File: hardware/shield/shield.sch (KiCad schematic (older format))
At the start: 30 parts, among them J10 10118193-0001LF, U1 LM1117, Y1 Crystal

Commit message: New version of shield.
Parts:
- removed C4: 22u, shield:SPARKFUN-CAPACITORS_AXIAL-5MM, symbol SPARKFUN-CAPACITORS_CAP
- removed R1, R2: 10k, shield:SPARKFUN-PASSIVES_0603-RES, symbol SPARKFUN-PASSIVES_RESISTOR
- removed U$2, U$3: TXS0101DBVR, shield:TEXAS_SOT-23-6, symbol TEXAS_TXS0101DBVR
- added C4: 22u, Capacitors_THT:C_Radial_D5_L6_P2.5, symbol CP
- added U2: 4052, Housings_SOIC:SOIC-16_3.9x9.9mm_Pitch1.27mm, symbol 4052
- added U3: TXB0104, Housings_SOIC:SOIC-14_3.9x8.7mm_Pitch1.27mm, symbol TXB0104
- JP1: value 3v3Src1 -> ~
- JP2: value 3v3Src2 -> ~
- PROG0: value PROG0 -> ~
- PROG1: value PROG1 -> ~
- PWR0: value PWR0 -> ~
- U$1: value CH340G -> ~
- Y1: value Crystal -> 12M
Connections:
- net labels added: D+, D-, RX, TX, XO
- net labels removed: N$1, N$3, N$43, N$46, N$49, N$5
- wire segments 193 -> 195
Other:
- moved on the sheet: E1

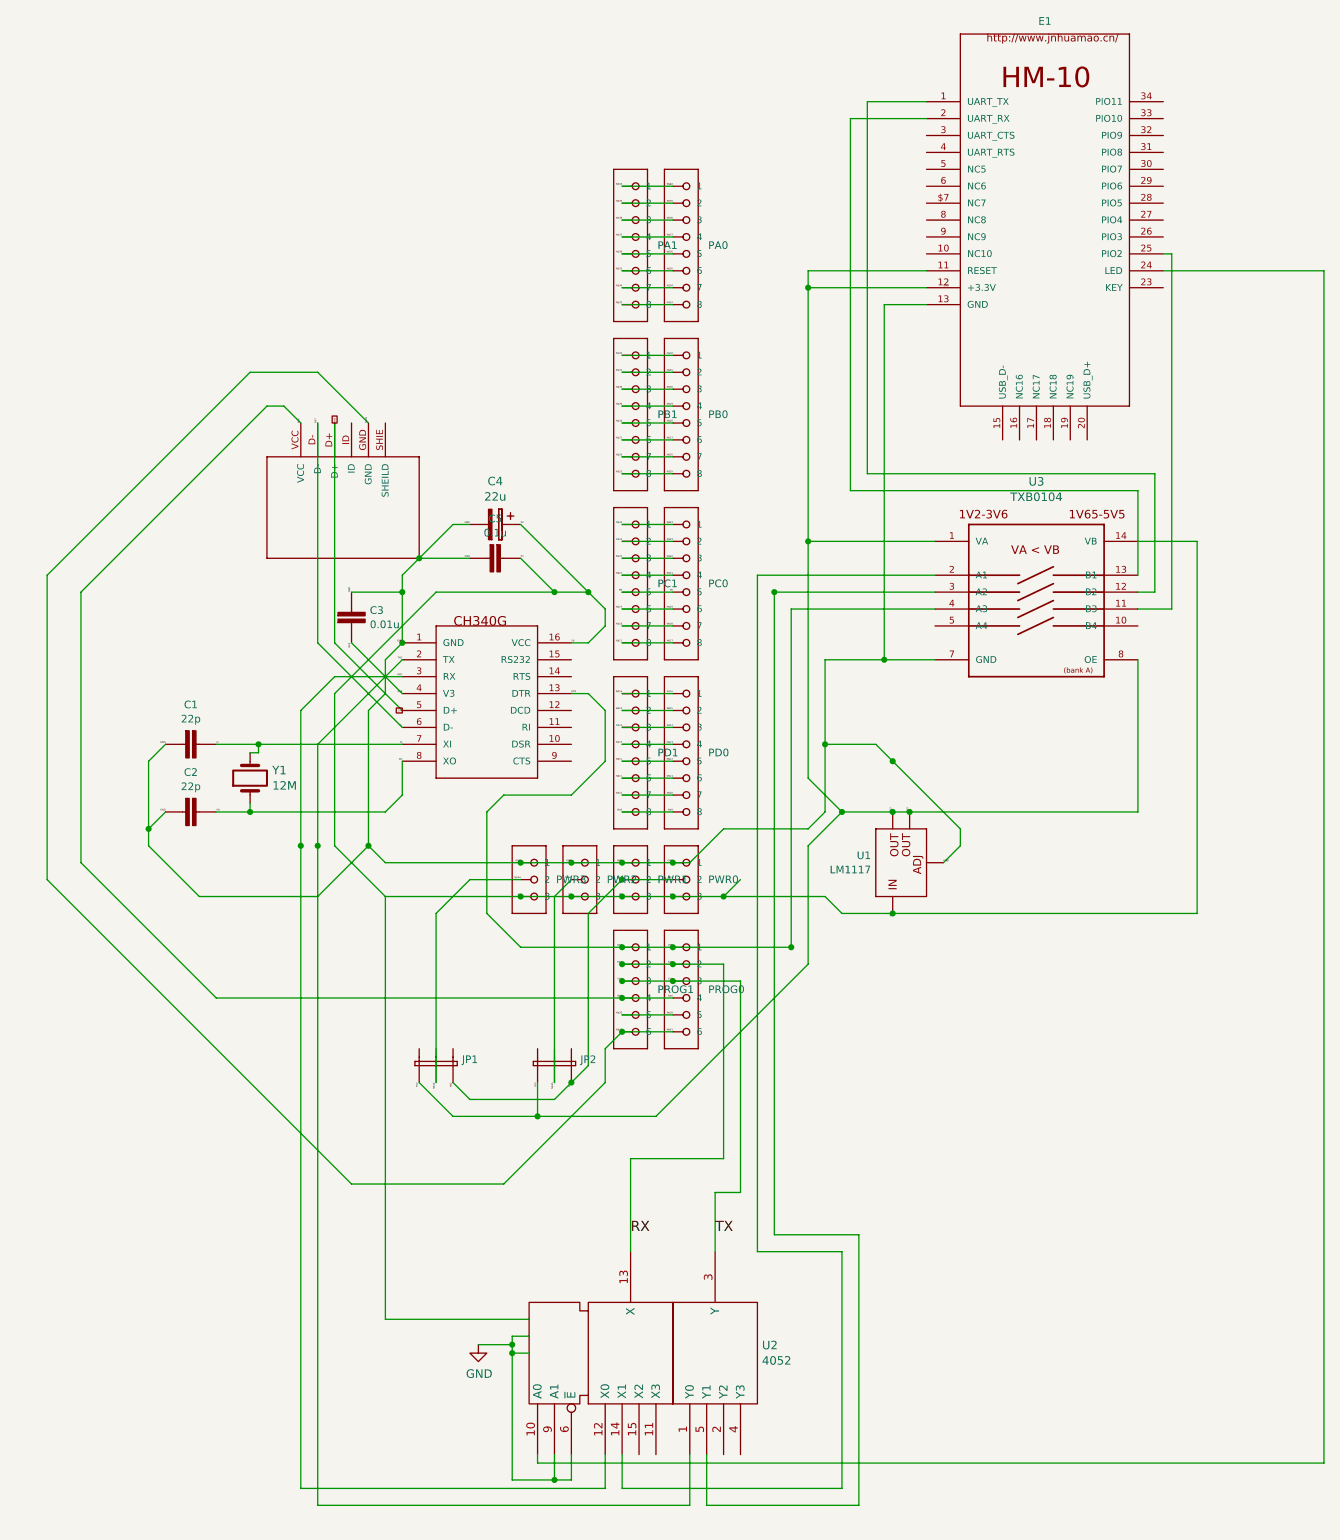
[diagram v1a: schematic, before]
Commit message: Fully-routed; just the wrong size.
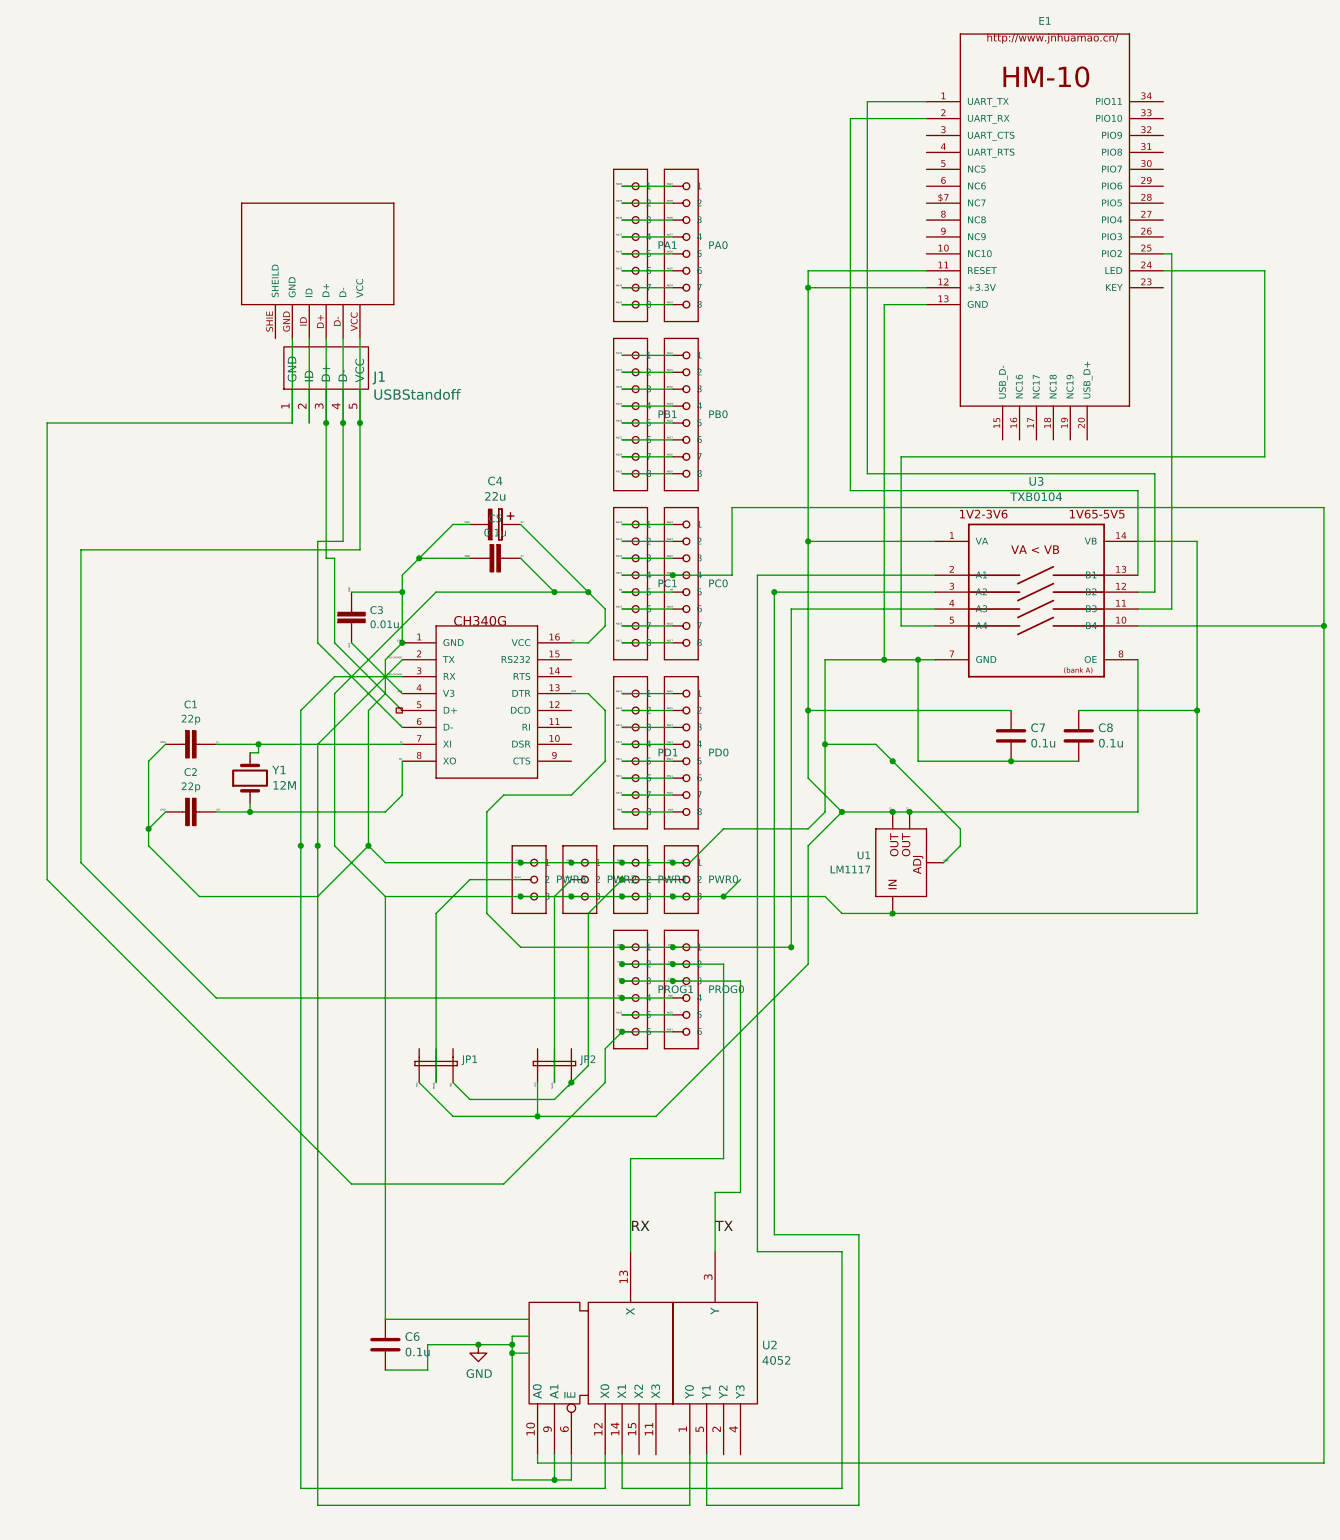
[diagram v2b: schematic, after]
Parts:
- added C6, C7, C8: 0.1u, Capacitors_SMD:C_0603_HandSoldering, symbol C
- added J1: USBStandoff, Pin_Headers:Pin_Header_Straight_1x05, symbol USBStandoff
- C1, C2, C3, C5: footprint shield:SPARKFUN-CAPACITORS_0603-CAP -> Capacitors_SMD:C_0603_HandSoldering
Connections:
- net 3V3: now also C7.1
- net D+: now also J1.3 (D+)
- net D-: now also J1.4 (D-)
- net GND: now also C6.2, C7.2, C8.2
- net N$21: now also U2.10 (A0), U3.10 (B4)
- net N$41: now also J1.1 (GND)
- net N$6: now also J1.5 (VCC)
- net RX: no longer U$1.3 (RX), U2.12 (X0)
- net TX: no longer U$1.2 (TX), U2.1 (Y0)
- net Vdd: now also C6.1, C8.1
- net at J10.ID: now also J1.2 (ID)
- net at E1.24 (LED): now also U3.5 (A4); no longer U2.10 (A0)
- new net RXD-CH340G: U$1.3 (RX), U2.12 (X0)
- new net TXD-CH340G: U$1.2 (TX), U2.1 (Y0)
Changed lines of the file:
@@
 L 10118193-0001LF_10118193-0001LF J10
 U 1 1 58543665
-P 9000 6550
-F 0 "J10" H 8990 6540 65  0001 L TNN
-F 1 "10118193-0001LF" H 8990 6440 65  0001 L TNN
-F 2 "shield:10118193-0001LF_10118193-0001LF" H 8990 6340 65  0001 L TNN
-F 3 "" H 9000 6550 60  0001 C CNN
-	1    9000 6550
-	0    -1   -1   0
+P 8950 5250
+F 0 "J10" H 8940 5240 65  0001 L TNN
+F 1 "10118193-0001LF" H 8940 5140 65  0001 L TNN
+F 2 "shield:10118193-0001LF_10118193-0001LF" H 8940 5040 65  0001 L TNN
+F 3 "" H 8950 5250 60  0001 C CNN
+	1    8950 5250
+	0    1    1    0
 $EndComp
 $Comp
@@
 Text GLabel 9400 7850 0    10   UnSpc ~ 0
 D+
-Text GLabel 9000 6150 1    10   UnSpc ~ 0
-N$4
 Text Label 9400 8150 2    10   ~ 0
 XO
@@
 Text Label 10700 9550 2    10   ~ 0
 N$6
-Text Label 8800 6150 1    10   ~ 0
-N$6
-Text Label 8900 6150 1    10   ~ 0
-N$7
 Text Label 9400 7950 2    10   ~ 0
 D-
@@
 Text Label 10700 9750 2    10   ~ 0
 N$41
-Text Label 9200 6150 1    10   ~ 0
-N$41
 Text Label 9600 10050 3    10   ~ 0
 N$44
@@
 RXD
 Text Label 9400 7650 2    10   ~ 0
-RXD
+RXD-CH340G
 Text Label 10700 9350 2    10   ~ 0
 RXD
@@
 TXD
 Text Label 9400 7550 2    10   ~ 0
-TXD
+TXD-CH340G
 Text Label 10700 9450 2    10   ~ 0
 TXD
@@
 F 0 "C3" H 9208 7442 45  0000 L CNN
 F 1 "0.01u" H 9208 7358 45  0000 L CNN
-F 2 "shield:SPARKFUN-CAPACITORS_0603-CAP" H 9100 7350 60  0001 C CNN
+F 2 "Capacitors_SMD:C_0603_HandSoldering" H 9100 7350 60  0001 C CNN
 F 3 "" H 9100 7350 60  0001 C CNN
 	1    9100 7350
@@
 F 0 "C5" V 9666 7000 45  0000 C CNN
 F 1 "0.1u" V 9750 7000 45  0000 C CNN
-F 2 "shield:SPARKFUN-CAPACITORS_0603-CAP" H 9900 6950 60  0001 C CNN
+F 2 "Capacitors_SMD:C_0603_HandSoldering" H 9900 6950 60  0001 C CNN
 F 3 "" H 9900 6950 60  0001 C CNN
 	1    9900 6950
@@
 F 0 "C1" V 7866 8100 45  0000 C CNN
 F 1 "22p" V 7950 8100 45  0000 C CNN
-F 2 "shield:SPARKFUN-CAPACITORS_0603-CAP" H 8100 8050 60  0001 C CNN
+F 2 "Capacitors_SMD:C_0603_HandSoldering" H 8100 8050 60  0001 C CNN
 F 3 "" H 8100 8050 60  0001 C CNN
 	1    8100 8050
@@
 F 0 "C2" V 7866 8500 45  0000 C CNN
 F 1 "22p" V 7950 8500 45  0000 C CNN
-F 2 "shield:SPARKFUN-CAPACITORS_0603-CAP" H 8100 8450 60  0001 C CNN
+F 2 "Capacitors_SMD:C_0603_HandSoldering" H 8100 8450 60  0001 C CNN
 F 3 "" H 8100 8450 60  0001 C CNN
 	1    8100 8450
@@
 	7300 8850 9100 10650
 Wire Wire Line
-	7300 7050 7300 8850
-Wire Wire Line
-	8500 5850 7300 7050
-Wire Wire Line
-	8900 5850 8500 5850
-Wire Wire Line
-	9200 6150 8900 5850
+	7300 6150 7300 8850
 Wire Wire Line
 	10700 9750 11000 9750
@@
 	10700 6950 11000 6950
 Wire Wire Line
-	11000 7050 10700 7050
+	10700 7050 11350 7050
 Wire Wire Line
 	10700 9650 11000 9650
@@
 Wire Wire Line
 	8900 7450 9400 7950
-Wire Wire Line
-	8900 6150 8900 7450
 Connection ~ 10700 9550
 Wire Wire Line
 	7500 8750 8300 9550
 Wire Wire Line
-	7500 7150 7500 8750
-Wire Wire Line
-	8600 6050 7500 7150
-Wire Wire Line
-	8700 6050 8600 6050
-Wire Wire Line
-	8800 6150 8700 6050
+	7500 6900 7500 8750
 Wire Wire Line
 	8300 9550 11000 9550
@@
 	8300 8450 9300 8450
 Wire Wire Line
-	9000 7450 9000 6150
-Wire Wire Line
-	9400 7850 9000 7450
+	9000 7450 9400 7850
 Wire Wire Line
 	8300 8050 9400 8050
@@
 	9300 11450 10150 11450
 Wire Wire Line
-	9850 11600 10050 11600
+	9550 11600 10050 11600
 Connection ~ 10050 11600
 Wire Wire Line
@@
 Wire Wire Line
 	10200 12300 14850 12300
-Wire Wire Line
-	14850 12300 14850 5250
 $Comp
 L CP C4
@@
 	11500 7050 11500 11050
 Wire Wire Line
-	14850 5250 13900 5250
-Wire Wire Line
 	13900 5150 13950 5150
 Wire Wire Line
@@
 	11800 5250 12500 5250
 Connection ~ 11800 5350
+$Comp
+L C C6
+U 1 1 585C607F
+P 9300 11600
+F 0 "C6" H 9415 11646 50  0000 L CNN
+F 1 "0.1u" H 9415 11555 50  0000 L CNN
+F 2 "Capacitors_SMD:C_0603_HandSoldering" H 9338 11450 50  0001 C CNN
+F 3 "" H 9300 11600 50  0000 C CNN
+	1    9300 11600
+	1    0    0    -1
+$EndComp
+Wire Wire Line
+	9300 11750 9550 11750
+Wire Wire Line
+	9550 11750 9550 11600
+Connection ~ 9850 11600
+$Comp
+L C C8
+U 1 1 585C65D3
+P 13400 8000
+F 0 "C8" H 13515 8046 50  0000 L CNN
+F 1 "0.1u" H 13515 7955 50  0000 L CNN
+F 2 "Capacitors_SMD:C_0603_HandSoldering" H 13438 7850 50  0001 C CNN
+F 3 "" H 13400 8000 50  0000 C CNN
+	1    13400 8000
+	1    0    0    -1
+$EndComp
+$Comp
+L C C7
+U 1 1 585C6655
+P 13000 8000
+F 0 "C7" H 13115 8046 50  0000 L CNN
+F 1 "0.1u" H 13115 7955 50  0000 L CNN
+F 2 "Capacitors_SMD:C_0603_HandSoldering" H 13038 7850 50  0001 C CNN
+F 3 "" H 13000 8000 50  0000 C CNN
+	1    13000 8000
+	1    0    0    -1
+$EndComp
+Wire Wire Line
+	13400 7850 14100 7850
+Connection ~ 14100 7850
+Wire Wire Line
+	13000 7850 11800 7850
+Connection ~ 11800 7850
+Wire Wire Line
+	12450 7550 12450 8150
+Wire Wire Line
+	12450 8150 13400 8150
+Connection ~ 12450 7550
+Connection ~ 13000 8150
+Wire Wire Line
+	13750 7350 14850 7350
+Connection ~ 14850 7350
+Wire Wire Line
+	14850 12300 14850 6650
+Wire Wire Line
+	13900 5250 14500 5250
+Wire Wire Line
+	14500 5250 14500 6350
+Wire Wire Line
+	14500 6350 12350 6350
+Wire Wire Line
+	12350 6350 12350 7350
+Wire Wire Line
+	12350 7350 12550 7350
+Wire Wire Line
+	11350 7050 11350 6650
+Wire Wire Line
+	11350 6650 14850 6650
+Connection ~ 11000 7050
+$Comp
+L USBStandoff J1
+U 1 1 585C9231
+P 9050 5950
+F 0 "J1" V 9122 5772 60  0000 R CNN
+F 1 "USBStandoff" V 9016 5772 60  0000 R CNN
+F 2 "Pin_Headers:Pin_Header_Straight_1x05" H 9050 5950 60  0001 C CNN
+F 3 "" H 9050 5950 60  0001 C CNN
+	1    9050 5950
+	0    -1   -1   0
+$EndComp
+Wire Wire Line
+	9150 6900 7500 6900
+Wire Wire Line
+	9150 5650 9150 6900
+Wire Wire Line
+	7300 6150 8750 6150
+Wire Wire Line
+	9000 6950 9000 7450
+Wire Wire Line
+	8950 6950 9000 6950
+Wire Wire Line
+	8950 5650 8950 6950
+Wire Wire Line
+	8900 7450 8900 6850
+Wire Wire Line
+	8900 6850 9050 6850
+Wire Wire Line
+	9050 6850 9050 5650
+Wire Wire Line
+	8750 6150 8750 5650
+Wire Wire Line
+	8850 6150 8850 5650
+Connection ~ 8950 6150
+Connection ~ 9050 6150
+Connection ~ 9150 6150
 $EndSCHEMATC

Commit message: Fully routed and with parts in reasonably OK spots.
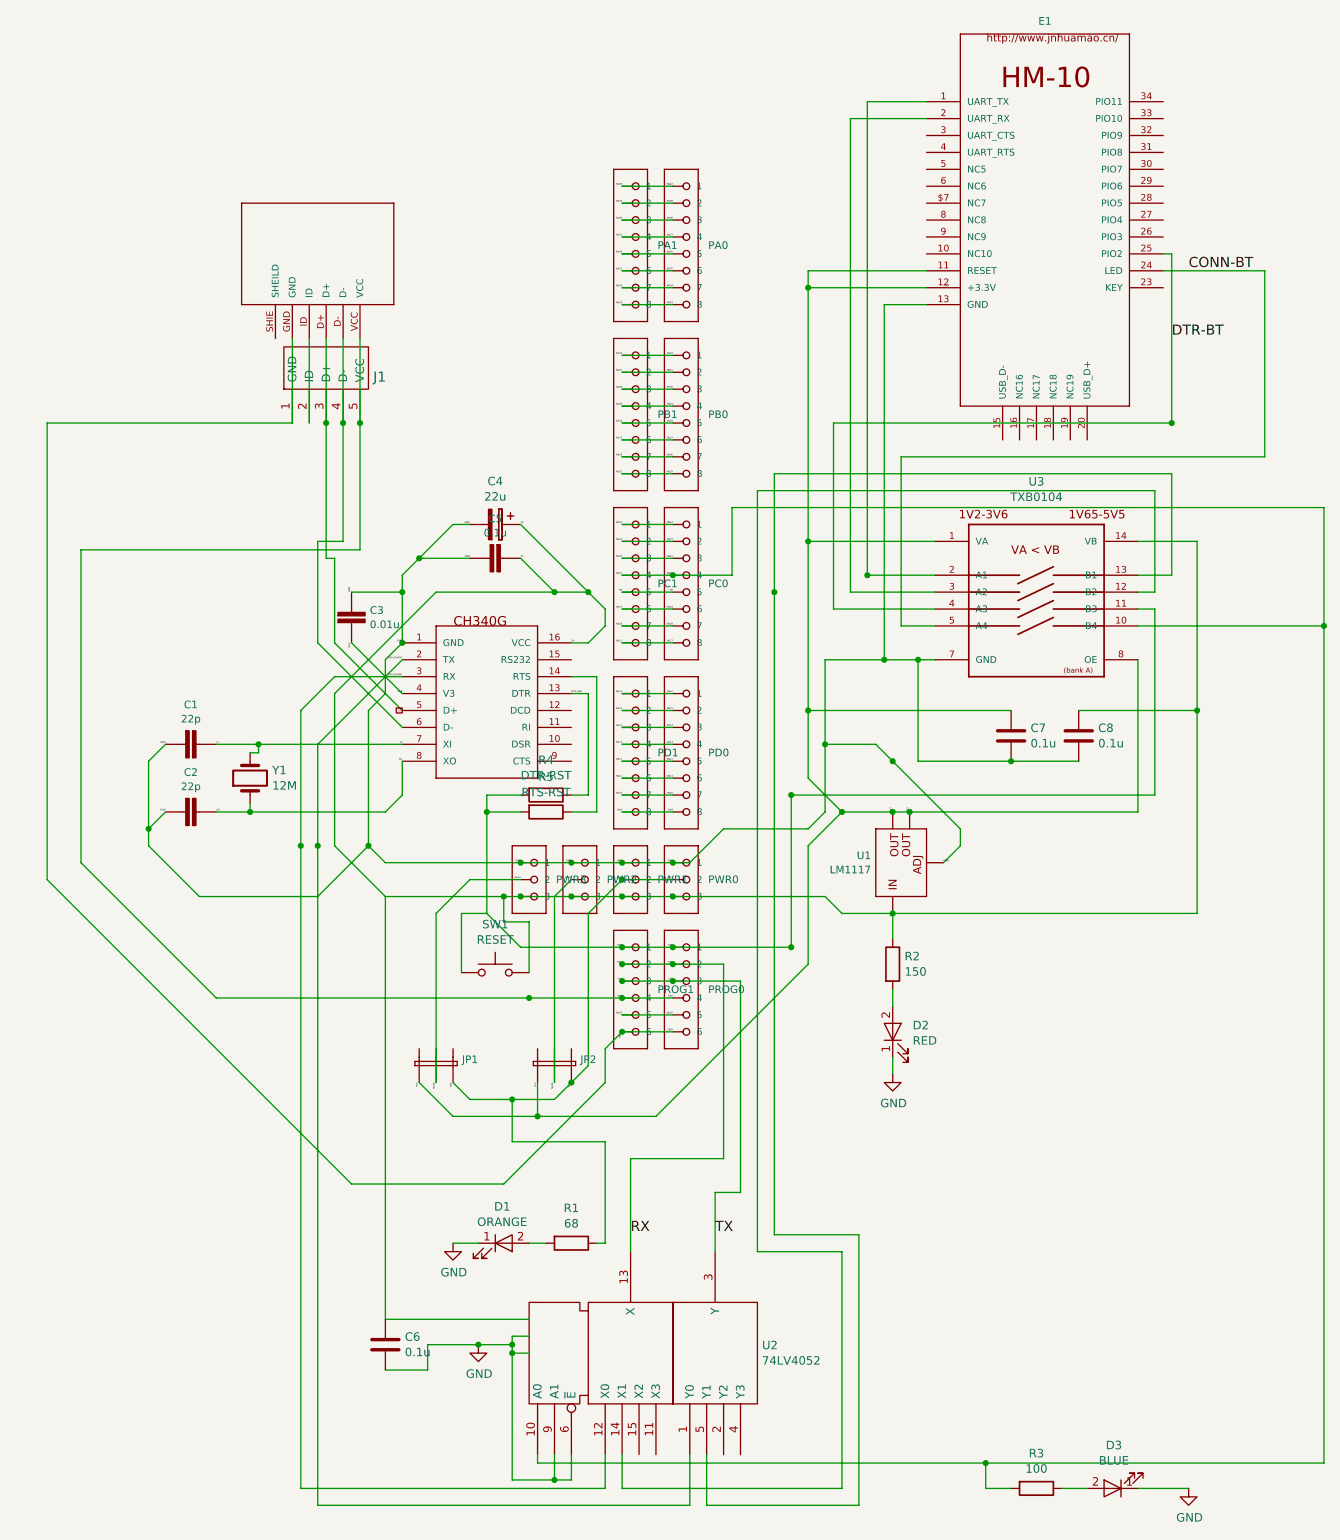
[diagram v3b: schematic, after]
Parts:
- added D1: ORANGE, LEDs:LED_0805, symbol LED
- added D2: RED, LEDs:LED_0805, symbol LED
- added D3: BLUE, LEDs:LED_0805, symbol LED
- added R1: 68, Resistors_SMD:R_0805_HandSoldering, symbol R
- added R2: 150, Resistors_SMD:R_0805_HandSoldering, symbol R
- added R3: 100, Resistors_SMD:R_0805_HandSoldering, symbol R
- added R4: DTR-RST, Capacitors_SMD:C_0805, symbol R
- added R5: RTS-RST, Capacitors_SMD:C_0805, symbol R
- added SW1: RESET, shield-pretty:NANO-SWITCH, symbol SW_Push
- C1, C2, C3, C5, C6, C7, C8: footprint Capacitors_SMD:C_0603_HandSoldering -> Capacitors_SMD:C_0805_HandSoldering
- J1: value USBStandoff -> ~
- PA0: value PA0 -> ~
- PA1: value PA1 -> ~
- PB0: value PB0 -> ~
- PB1: value PB1 -> ~
- PC0: value PC0 -> ~
- PC1: value PC1 -> ~
- PD0: value PD0 -> ~
- PD1: value PD1 -> ~
- PWR1: value PWR1 -> ~
- PWR2: value PWR2 -> ~
- PWR3: value PWR3 -> ~
- U2: value 4052 -> 74LV4052
- Y1: footprint Crystals:HC-49V -> Crystals:Crystal_HC49-U_Vertical
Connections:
- net N$41 is gone; now on net GND: J1.1 (GND), J10.GND, PROG0.6, PROG1.6
- net DTR: now also U3.11 (B3), R4.2, R5.2, SW1.1; no longer U$1.13 (DTR), U3.4 (A3)
- net GND: now also D1.1 (K), D2.1 (K), D3.1 (K)
- net N$2: now also R1.1
- net N$21: now also R3.2
- net Vdd: now also R2.1, SW1.2
- net at U$1.14 (RTS): now also R5.1
- net at E1.1 (UART_TX): now also U3.2 (A1); no longer U3.12 (B2)
- net at E1.2 (UART_RX): now also U3.3 (A2); no longer U3.13 (B1)
- net CONN-BT: now reaches E1.24 (LED), U3.5 (A4)
- net DTR-BT: now reaches E1.25 (PIO2)
- net DTR-BT: now also U3.4 (A3); no longer U3.11 (B3)
- net at U2.14 (X1): now also U3.12 (B2); no longer U3.2 (A1)
- net at U2.5 (Y1): now also U3.13 (B1); no longer U3.3 (A2)
- new net: D3.2 (A), R3.1
- new net: D2.2 (A), R2.2
- new net: D1.2 (A), R1.2
- new net DTR-USB: R4.1, U$1.13 (DTR)
